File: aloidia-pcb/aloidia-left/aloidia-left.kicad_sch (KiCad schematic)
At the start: 225 parts, among them J1 SWD_02x05_1.27mm, J10 Pin headers 2.54mm 01x02, J11 USB4105-GF-A-120, J12 Pin headers 2.54mm 01x08, J2 Pin headers 2.54mm 01x08, J3 SM06B-SRSS-TB, J4 SM03B-SRSS-TB(LF)(SN), J5 S2B-PH-SM4-TB(LF)(SN), J6 Pin headers 2.54mm 01x03, J7 USB4105-GF-A-120, J9 S2B-PH-SM4-TB(LF)(SN), Q1 PJA3404, Q2 DMG9926UDM, Q3 Si2371EDS, Q4 Si2371EDS, Q5 PJA3404, SW1 SSSS213100, SW100 MX_EC11, SW101 SW_Push, SW102 SW_Push, SW103 SW_Push, SW104 SW_Push, SW105 SW_Push, SW106 SW_Push, SW107 SW_Push, SW108 SW_Push, SW110 SW_Push, SW111 SW_Push, SW112 SW_Push, SW113 SW_Push, SW114 SW_Push, SW115 SW_Push, SW116 SW_Push, SW117 SW_Push, SW120 SW_Push, SW121 SW_Push, SW122 SW_Push, SW123 SW_Push, SW124 SW_Push, SW125 SW_Push, SW126 SW_Push, SW127 SW_Push, SW130 SW_Push, SW131 SW_Push, SW132 SW_Push, SW133 SW_Push, SW134 SW_Push, SW135 SW_Push, SW136 SW_Push, SW137 SW_Push, SW140 SW_Push, SW141 SW_Push, SW142 SW_Push, SW143 SW_Push, SW144 SW_Push, SW145 SW_Push, SW146 SW_Push, SW2 MX_EVQWGD001, SW243 SW_Push, SW244 SW_Push, SW246 SW_Push, SW4 EG6201, U1 MAX17048, U2 MDBT50Q-1MV2, U3 MCP1812AT-033/TT, U4 DMN2004DMK-7, U5 BQ24075RGT, U6 AP9101CK6-ANTRG1, U7 STS234050UL30, U8 BQ25504, U9 LTC4359-MS8, Y1 32.768kHz

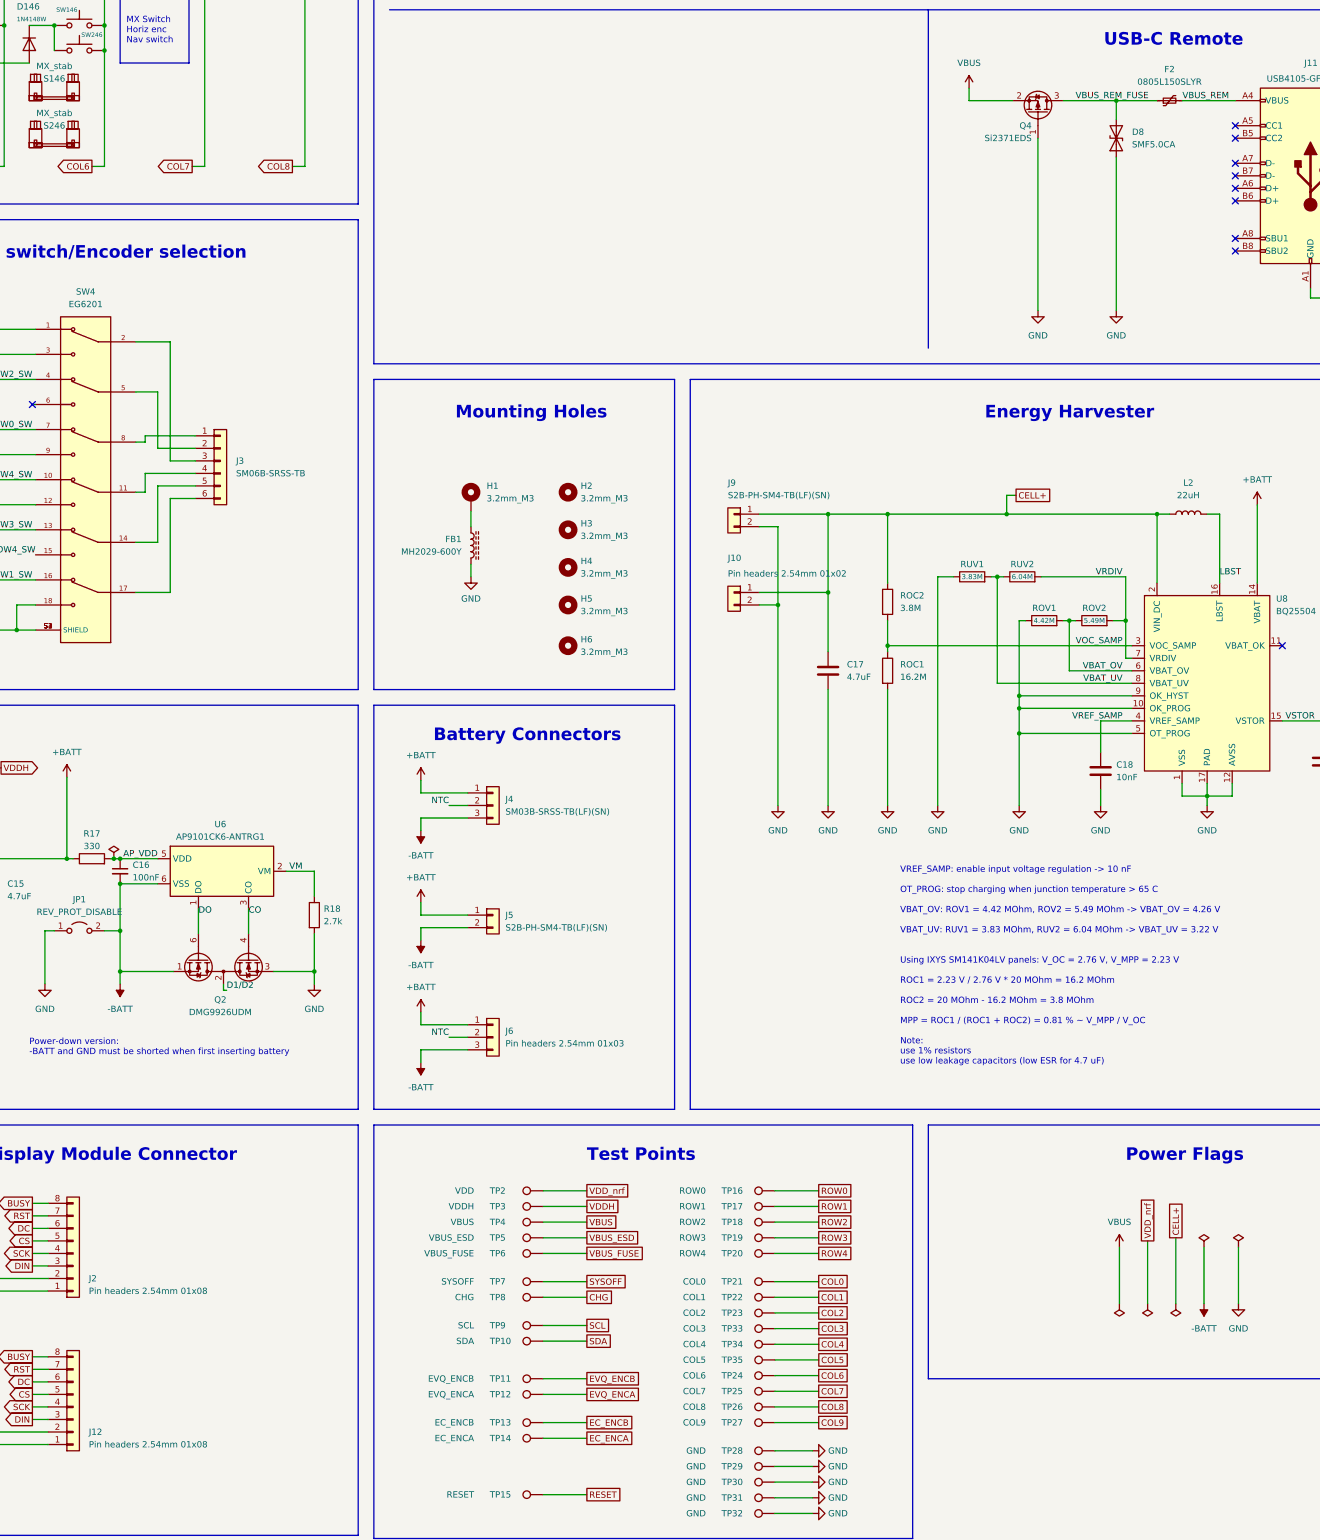
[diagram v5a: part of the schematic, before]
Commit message: Changed connectors to jst-sh
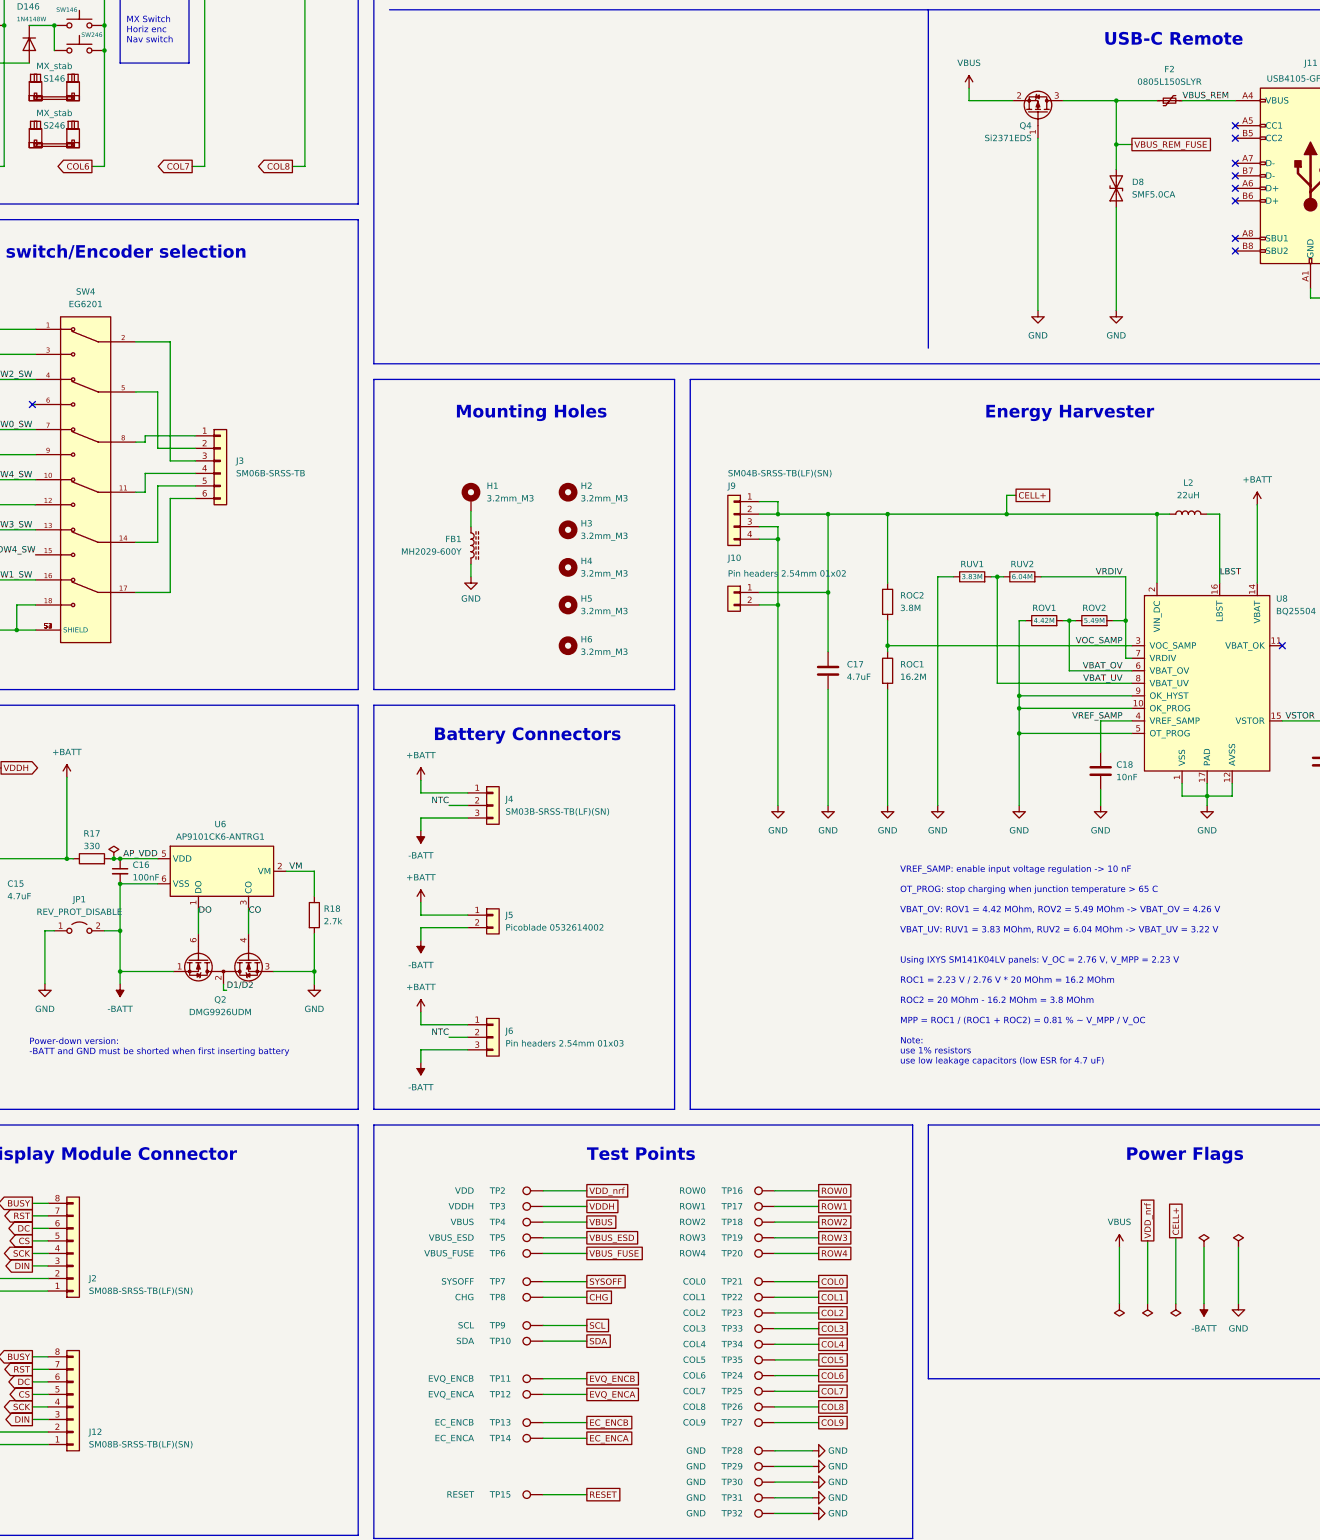
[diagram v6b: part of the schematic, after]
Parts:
- removed J9: S2B-PH-SM4-TB(LF)(SN), Connector_JST:JST_PH_S2B-PH-SM4-TB_1x02-1MP_P2.00mm_Horizontal, symbol Connector_Generic:Conn_01x02
- added J9: SM04B-SRSS-TB(LF)(SN), Connector_JST:JST_SH_SM04B-SRSS-TB_1x04-1MP_P1.00mm_Horizontal, symbol Connector_Generic:Conn_01x04
- J12, J2: value Pin headers 2.54mm 01x08 -> SM08B-SRSS-TB(LF)(SN); footprint 0_various:e-Paper Display -> Connector_JST:JST_SH_SM08B-SRSS-TB_1x08-1MP_P1.00mm_Horizontal
- J5: value S2B-PH-SM4-TB(LF)(SN) -> Picoblade 0532614002; footprint Connector_JST:JST_PH_S2B-PH-SM4-TB_1x02-1MP_P2.00mm_Horizontal -> Connector_Molex:Molex_PicoBlade_53261-0271_1x02-1MP_P1.25mm_Horizontal; Digikey ref (none) -> 900-0532614002CT-ND; Manufacturer ref (none) -> 0532614002
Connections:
- net CELL+: now also J9.1 (Pin_1), J9.2 (Pin_2)
- net GND: now also J9.3 (Pin_3), J9.4 (Pin_4)
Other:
- moved on the sheet: D8

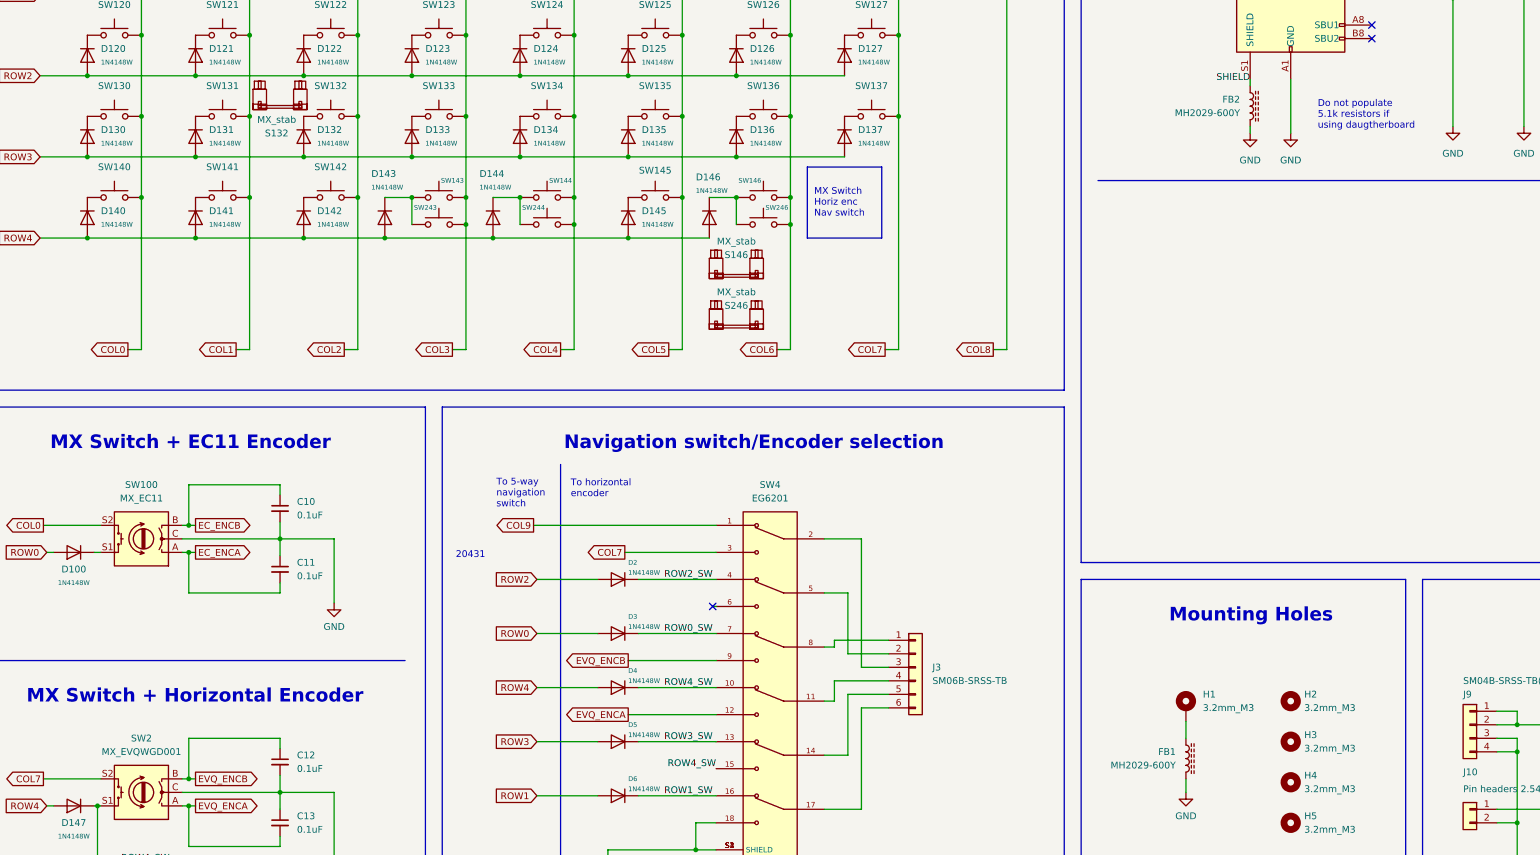
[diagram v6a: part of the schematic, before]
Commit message: Adjusted trace widths
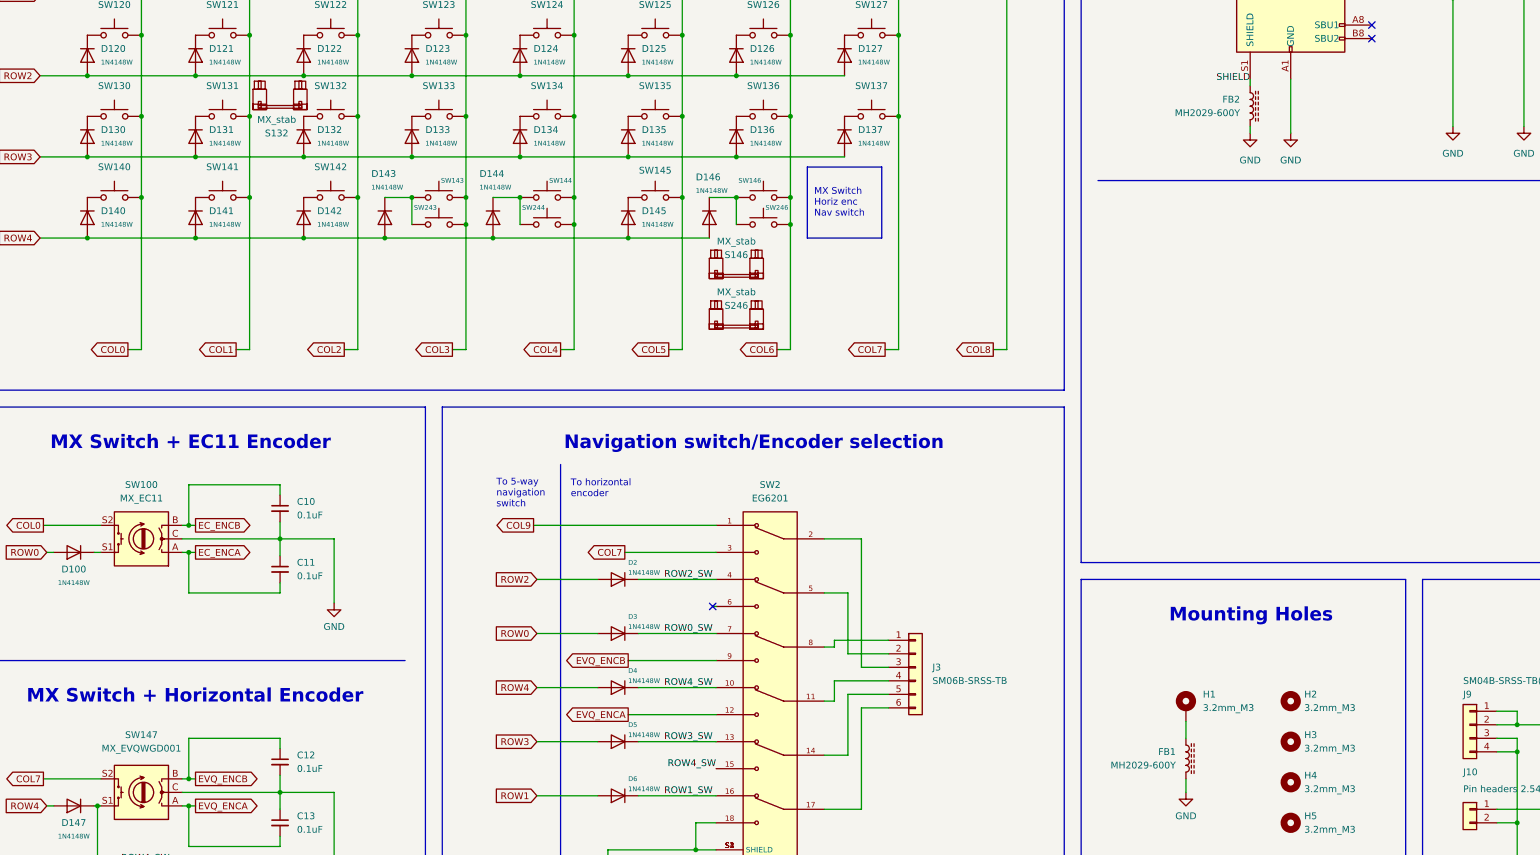
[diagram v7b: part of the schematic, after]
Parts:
- renumbered SW2 to SW147, SW4 to SW2
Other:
- note removed: "20431"
- note removed: "Do not populate 5.1k resistors if using daugtherboard"
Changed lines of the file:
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@@
     (effects (font (size 2.54 2.54) (thickness 0.508) bold) (justify left bottom))
   )
-  (text "20431" (at 244.475 166.37 0)
-    (effects (font (size 1.27 1.27)) (justify left bottom))
-  )
   (text "Test Points" (at 405.13 328.93 0)
     (effects (font (size 2.54 2.54) (thickness 0.508) bold) (justify left bottom))
@@
     (effects (font (size 1.27 1.27)) (justify left bottom))
   )
-  (text "Do not populate \n5.1k resistors if\nusing daugtherboard"
-    (at 406.4 85.725 0)
-    (effects (font (size 1.27 1.27)) (justify left bottom))
-  )
   (text "3.3V LDO" (at 106.68 243.84 0)
     (effects (font (size 2.54 2.54) (thickness 0.508) bold) (justify left bottom))
@@
   (symbol (lib_id "Device:RotaryEncoder_Switch") (at 185.42 210.185 180) (unit 1)
     (in_bom yes) (on_board yes) (fields_autoplaced)
-    (property "Reference" "SW2" (id 0) (at 185.42 200.025 0))
-    (property "Value" "MX_EVQWGD001" (id 1) (at 185.42 202.565 0))
+    (property "Reference" "SW147" (id 0) (at 185.42 199.39 0))
+    (property "Value" "MX_EVQWGD001" (id 1) (at 185.42 201.93 0))
     (property "Footprint" "0_mx:MX_HS_AS_1u_EVQWGD001" (id 2) (at 189.23 214.249 0)
       (effects (font (size 1.27 1.27)) hide)
@@
   (symbol (lib_id "0_switch_button:EG6201") (at 303.53 187.96 0) (mirror y) (unit 1)
     (in_bom yes) (on_board yes) (fields_autoplaced)
-    (property "Reference" "SW4" (id 0) (at 303.53 152.4 0))
+    (property "Reference" "SW2" (id 0) (at 303.53 152.4 0))
     (property "Value" "EG6201" (id 1) (at 303.53 154.94 0))
     (property "Footprint" "0_switch_button:SW_EG6201" (id 2) (at 303.53 187.96 0)
@@
       (reference "SW1") (unit 1) (value "SSSS213100") (footprint "marbastlib-various:SW_SSSS213100")
     )
-    (path "/02255a2e-cf6a-4aaf-b567-b14904a1768b"
-      (reference "SW2") (unit 1) (value "MX_EVQWGD001") (footprint "0_mx:MX_HS_AS_1u_EVQWGD001")
-    )
     (path "/3fe6fed8-9a07-421e-99c1-11871056c590"
-      (reference "SW4") (unit 1) (value "EG6201") (footprint "0_switch_button:SW_EG6201")
+      (reference "SW2") (unit 1) (value "EG6201") (footprint "0_switch_button:SW_EG6201")
     )
     (path "/6758c029-d18f-4e53-a4f0-ea56f0ed8397"
@@
       (reference "SW146") (unit 1) (value "SW_Push") (footprint "0_mx:MX_HS_AS_1u")
     )
+    (path "/02255a2e-cf6a-4aaf-b567-b14904a1768b"
+      (reference "SW147") (unit 1) (value "MX_EVQWGD001") (footprint "0_mx:MX_HS_AS_1u_EVQWGD001")
+    )
     (path "/f82dd2b9-8a0e-4acd-880a-7e176fcd0b3a"
